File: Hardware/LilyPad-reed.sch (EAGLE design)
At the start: 6 parts

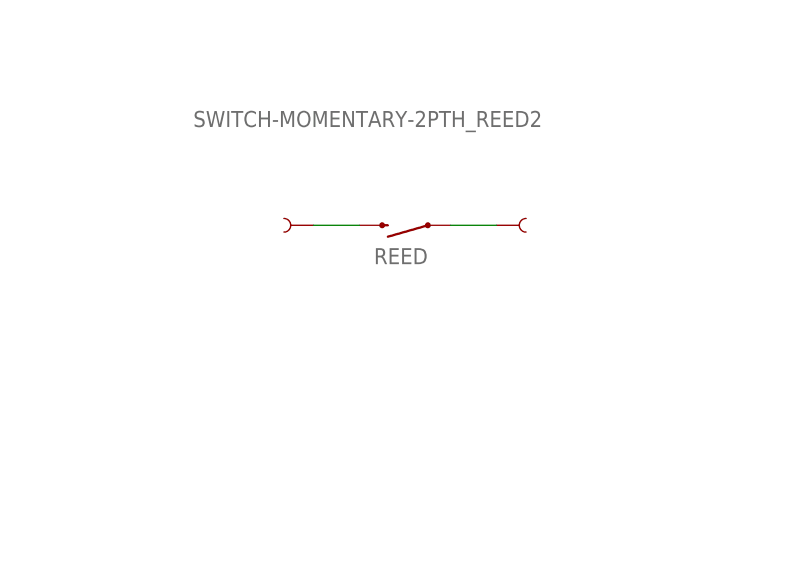
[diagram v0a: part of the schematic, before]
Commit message: post-review edits
added PTH pins
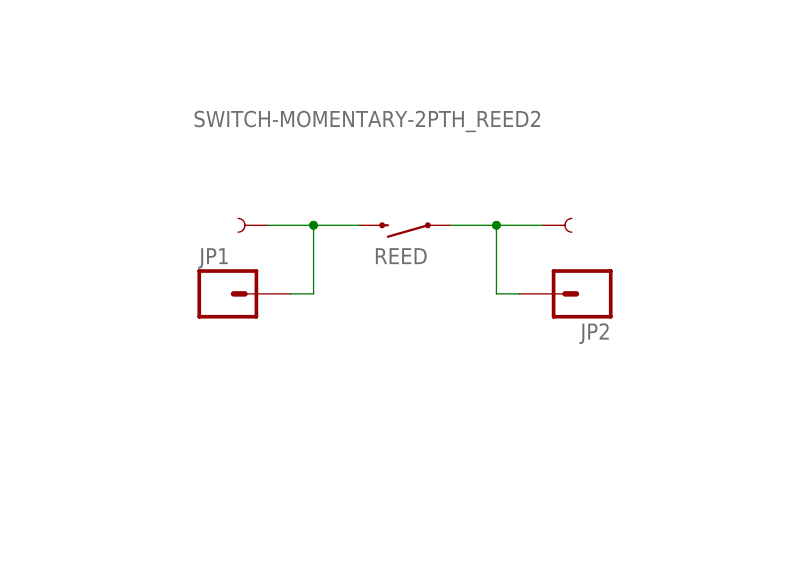
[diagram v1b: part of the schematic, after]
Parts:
- added JP1, JP2: (no value), SparkFun-Connectors:M01PTH
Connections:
- net N$1: now also JP1.1
- net N$2: now also JP2.1
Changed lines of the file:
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@@
 <layer number="56" name="wert" color="7" fill="1" visible="no" active="no"/>
 <layer number="57" name="tCAD" color="7" fill="1" visible="no" active="no"/>
+<layer number="90" name="Modules" color="5" fill="1" visible="yes" active="yes"/>
 <layer number="91" name="Nets" color="2" fill="1" visible="yes" active="yes"/>
 <layer number="92" name="Busses" color="1" fill="1" visible="yes" active="yes"/>
@@
 <part name="U$1" library="LilyPad-Wearables" deviceset="LOGO-LP" device="LP"/>
 <part name="LOGO1" library="SparkFun-Aesthetics" deviceset="OSHW-LOGO" device="S"/>
+<part name="JP1" library="SparkFun-Connectors" deviceset="M01" device="PTH"/>
+<part name="JP2" library="SparkFun-Connectors" deviceset="M01" device="PTH"/>
 </parts>
 <sheets>
@@
 <instance part="FRAME1" gate="G$1" x="0" y="0"/>
 <instance part="FRAME1" gate="V" x="147.32" y="0"/>
-<instance part="SLIDEOFF" gate="G$1" x="114.3" y="96.52" rot="R180"/>
-<instance part="SLIDEON" gate="G$1" x="139.7" y="96.52"/>
+<instance part="SLIDEOFF" gate="G$1" x="109.22" y="96.52" rot="R180"/>
+<instance part="SLIDEON" gate="G$1" x="144.78" y="96.52"/>
 <instance part="REED" gate="G$1" x="127" y="96.52" smashed="yes" rot="R180">
 <attribute name="NAME" x="129.54" y="93.98" size="1.778" layer="95" rot="R180"/>
@@
 <instance part="U$1" gate="G$1" x="233.68" y="27.94"/>
 <instance part="LOGO1" gate="G$1" x="127" y="15.24"/>
+<instance part="JP1" gate="G$1" x="106.68" y="88.9"/>
+<instance part="JP2" gate="G$1" x="147.32" y="88.9" rot="R180"/>
 </instances>
 <busses>
@@
 <pinref part="SLIDEOFF" gate="G$1" pin="1"/>
 <pinref part="REED" gate="G$1" pin="2"/>
+<wire x1="111.76" y1="96.52" x2="116.84" y2="96.52" width="0.1524" layer="91"/>
+<pinref part="JP1" gate="G$1" pin="1"/>
 <wire x1="116.84" y1="96.52" x2="121.92" y2="96.52" width="0.1524" layer="91"/>
+<wire x1="114.3" y1="88.9" x2="116.84" y2="88.9" width="0.1524" layer="91"/>
+<wire x1="116.84" y1="88.9" x2="116.84" y2="96.52" width="0.1524" layer="91"/>
+<junction x="116.84" y="96.52"/>
 </segment>
 </net>
@@
 <pinref part="SLIDEON" gate="G$1" pin="1"/>
 <wire x1="132.08" y1="96.52" x2="137.16" y2="96.52" width="0.1524" layer="91"/>
+<pinref part="JP2" gate="G$1" pin="1"/>
+<wire x1="137.16" y1="96.52" x2="142.24" y2="96.52" width="0.1524" layer="91"/>
+<wire x1="139.7" y1="88.9" x2="137.16" y2="88.9" width="0.1524" layer="91"/>
+<wire x1="137.16" y1="88.9" x2="137.16" y2="96.52" width="0.1524" layer="91"/>
+<junction x="137.16" y="96.52"/>
 </segment>
 </net>

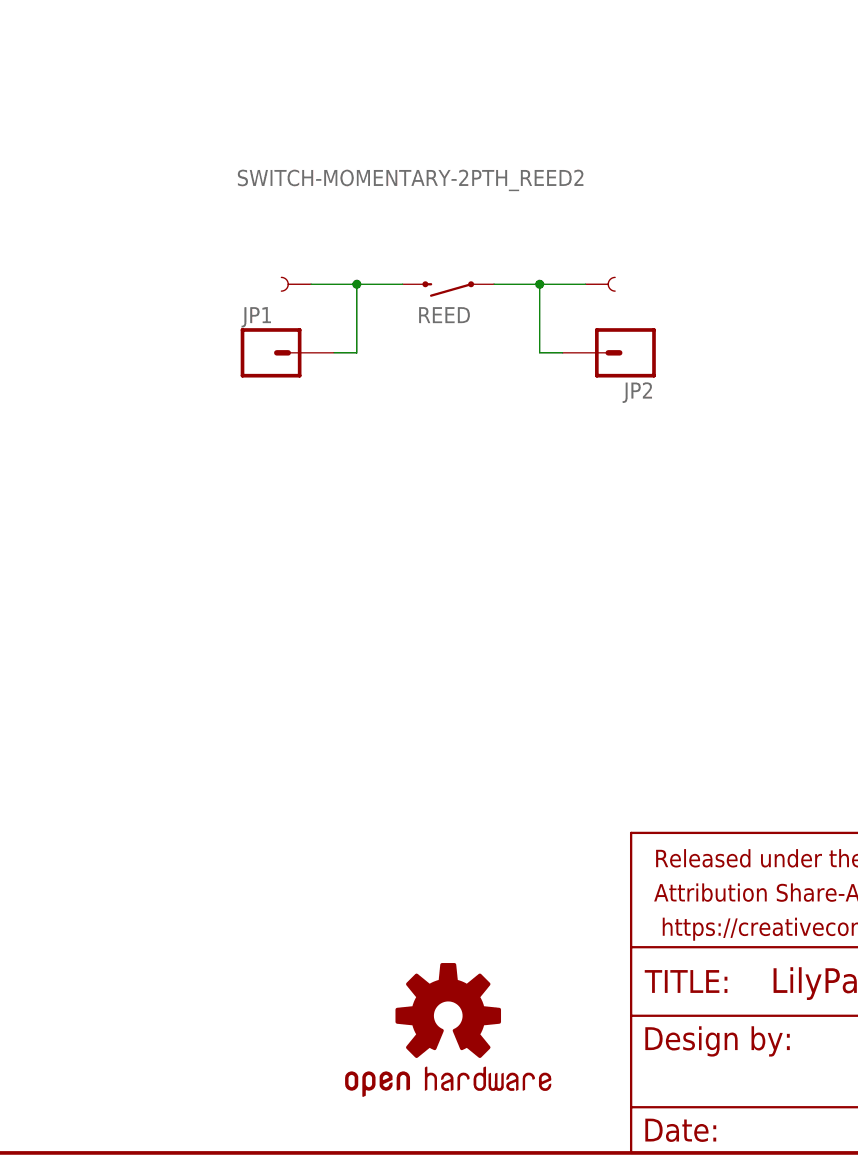
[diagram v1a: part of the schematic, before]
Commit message: Increased trace width, added dimension
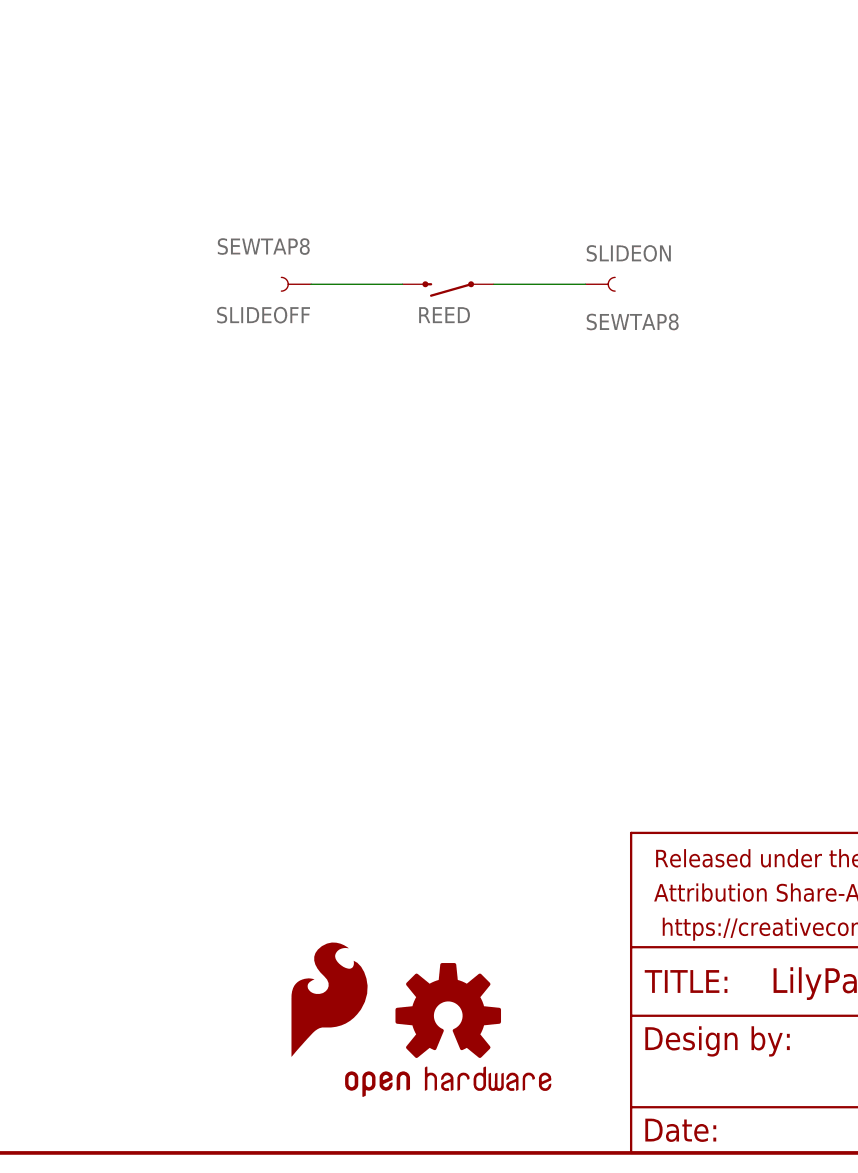
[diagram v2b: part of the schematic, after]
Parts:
- removed JP1, JP2: (no value), SparkFun-Connectors:M01PTH
- added LOGO2: SFE_LOGO_FLAME.1COP, SparkFun-Aesthetics:SFE_LOGO_FLAME.1COP
- LOGO1: value OSHW-LOGOS -> OSHW-LOGOS-COPPER; device SparkFun-Aesthetics:OSHW-LOGOS -> SparkFun-Aesthetics:OSHW-LOGOS-COPPER
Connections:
- net N$1: no longer JP1.1
- net N$2: no longer JP2.1
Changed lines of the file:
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@@
 <layer number="56" name="wert" color="7" fill="1" visible="no" active="no"/>
 <layer number="57" name="tCAD" color="7" fill="1" visible="no" active="no"/>
+<layer number="59" name="tCarbon" color="7" fill="1" visible="no" active="no"/>
+<layer number="60" name="bCarbon" color="7" fill="1" visible="no" active="no"/>
 <layer number="90" name="Modules" color="5" fill="1" visible="yes" active="yes"/>
 <layer number="91" name="Nets" color="2" fill="1" visible="yes" active="yes"/>
@@
 <layer number="127" name="_tValues" color="7" fill="1" visible="no" active="yes"/>
 <layer number="128" name="_bValues" color="7" fill="1" visible="no" active="yes"/>
+<layer number="129" name="Mask" color="7" fill="1" visible="yes" active="yes"/>
 <layer number="131" name="tAdjust" color="7" fill="1" visible="no" active="yes"/>
 <layer number="132" name="bAdjust" color="7" fill="1" visible="no" active="yes"/>
@@
 <layer number="251" name="SMDround" color="12" fill="11" visible="no" active="no"/>
 <layer number="254" name="cooling" color="7" fill="1" visible="yes" active="yes"/>
+<layer number="255" name="routoute" color="7" fill="1" visible="yes" active="yes"/>
 </layers>
 <schematic xreflabel="%F%N/%S" xrefpart="/%S.%C%R">
@@
 <part name="REED" library="SparkFun-Electromechanical" deviceset="SWITCH-MOMENTARY-2" device="PTH_REED2"/>
 <part name="U$1" library="LilyPad-Wearables" deviceset="LOGO-LP" device="LP"/>
-<part name="LOGO1" library="SparkFun-Aesthetics" deviceset="OSHW-LOGO" device="S"/>
-<part name="JP1" library="SparkFun-Connectors" deviceset="M01" device="PTH"/>
-<part name="JP2" library="SparkFun-Connectors" deviceset="M01" device="PTH"/>
+<part name="LOGO1" library="SparkFun-Aesthetics" deviceset="OSHW-LOGO" device="S-COPPER"/>
+<part name="LOGO2" library="SparkFun-Aesthetics" deviceset="SFE_LOGO_FLAME" device=".1COP" value="SFE_LOGO_FLAME.1COP"/>
 </parts>
 <sheets>
@@
 <instance part="REED" gate="G$1" x="127" y="96.52" smashed="yes" rot="R180">
 <attribute name="NAME" x="129.54" y="93.98" size="1.778" layer="95" rot="R180"/>
-<attribute name="VALUE" x="142.24" y="109.22" size="1.778" layer="96" rot="R180"/>
 </instance>
 <instance part="U$1" gate="G$1" x="233.68" y="27.94"/>
 <instance part="LOGO1" gate="G$1" x="127" y="15.24"/>
-<instance part="JP1" gate="G$1" x="106.68" y="88.9"/>
-<instance part="JP2" gate="G$1" x="147.32" y="88.9" rot="R180"/>
+<instance part="LOGO2" gate="G$1" x="109.22" y="10.16"/>
 </instances>
 <busses>
@@
 <pinref part="SLIDEOFF" gate="G$1" pin="1"/>
 <pinref part="REED" gate="G$1" pin="2"/>
-<wire x1="111.76" y1="96.52" x2="116.84" y2="96.52" width="0.1524" layer="91"/>
-<pinref part="JP1" gate="G$1" pin="1"/>
-<wire x1="116.84" y1="96.52" x2="121.92" y2="96.52" width="0.1524" layer="91"/>
-<wire x1="114.3" y1="88.9" x2="116.84" y2="88.9" width="0.1524" layer="91"/>
-<wire x1="116.84" y1="88.9" x2="116.84" y2="96.52" width="0.1524" layer="91"/>
-<junction x="116.84" y="96.52"/>
+<wire x1="111.76" y1="96.52" x2="121.92" y2="96.52" width="0.1524" layer="91"/>
 </segment>
 </net>
@@
 <pinref part="REED" gate="G$1" pin="1"/>
 <pinref part="SLIDEON" gate="G$1" pin="1"/>
-<wire x1="132.08" y1="96.52" x2="137.16" y2="96.52" width="0.1524" layer="91"/>
-<pinref part="JP2" gate="G$1" pin="1"/>
-<wire x1="137.16" y1="96.52" x2="142.24" y2="96.52" width="0.1524" layer="91"/>
-<wire x1="139.7" y1="88.9" x2="137.16" y2="88.9" width="0.1524" layer="91"/>
-<wire x1="137.16" y1="88.9" x2="137.16" y2="96.52" width="0.1524" layer="91"/>
-<junction x="137.16" y="96.52"/>
+<wire x1="132.08" y1="96.52" x2="142.24" y2="96.52" width="0.1524" layer="91"/>
 </segment>
 </net>
